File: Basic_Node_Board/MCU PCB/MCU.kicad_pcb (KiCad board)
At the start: 4 copper layers, 100 x 100 mm, 31 parts, among them J1 Conn_01x02, J2 Conn_01x06_Socket, J4 Conn_01x02_Pin, J5 Conn_01x03_Socket, U2 ESP32-DEVKIT-C, U3 TPS54560BQDDARQ1, U6 TJA1050T/CM,118

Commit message: fixed the buck converter
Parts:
- added REF**: MountingHole_3.2mm_M3_DIN965_Pad_TopBottom, MountingHole:MountingHole_3.2mm_M3_DIN965_Pad_TopBottom, F.Cu at (39.8, 120.8)
- added REF**: MountingHole_3.2mm_M3_DIN965_Pad_TopBottom, MountingHole:MountingHole_3.2mm_M3_DIN965_Pad_TopBottom, F.Cu at (131.8, 28.5)
- added REF**: MountingHole_3.2mm_M3_DIN965_Pad_TopBottom, MountingHole:MountingHole_3.2mm_M3_DIN965_Pad_TopBottom, F.Cu at (131.0, 120.2)
- moved L1 13.8 mm to (76.0, 41.8)
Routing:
- net Net-(U3-FB): track 34.2 -> 52.6 mm, vias 2 -> 3
- net Net-(U3-SW): track 17.8 -> 24.6 mm, vias 0 -> 2
- net 5.3V OUT: track 264.1 -> 270.0 mm, vias 4 -> 6
- net Net-(J3-Pin_12): track 120.4 -> 116.8 mm

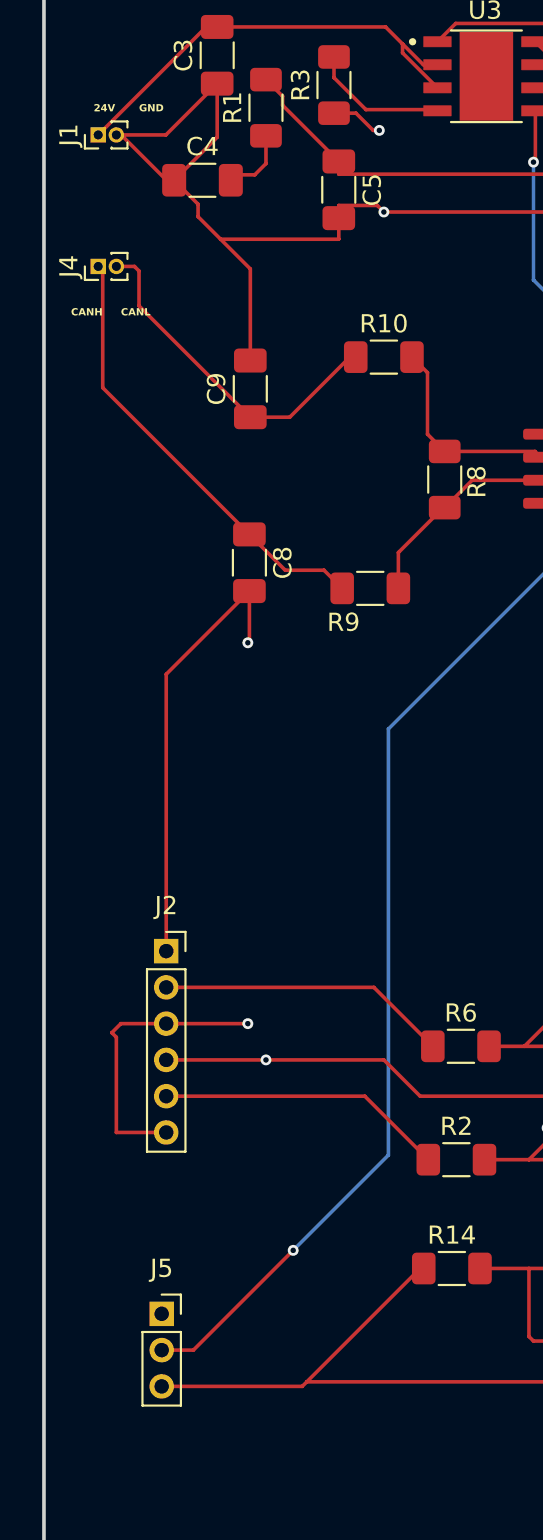
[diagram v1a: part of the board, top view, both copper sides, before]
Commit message: fixed the pin and connectors for the mcu board
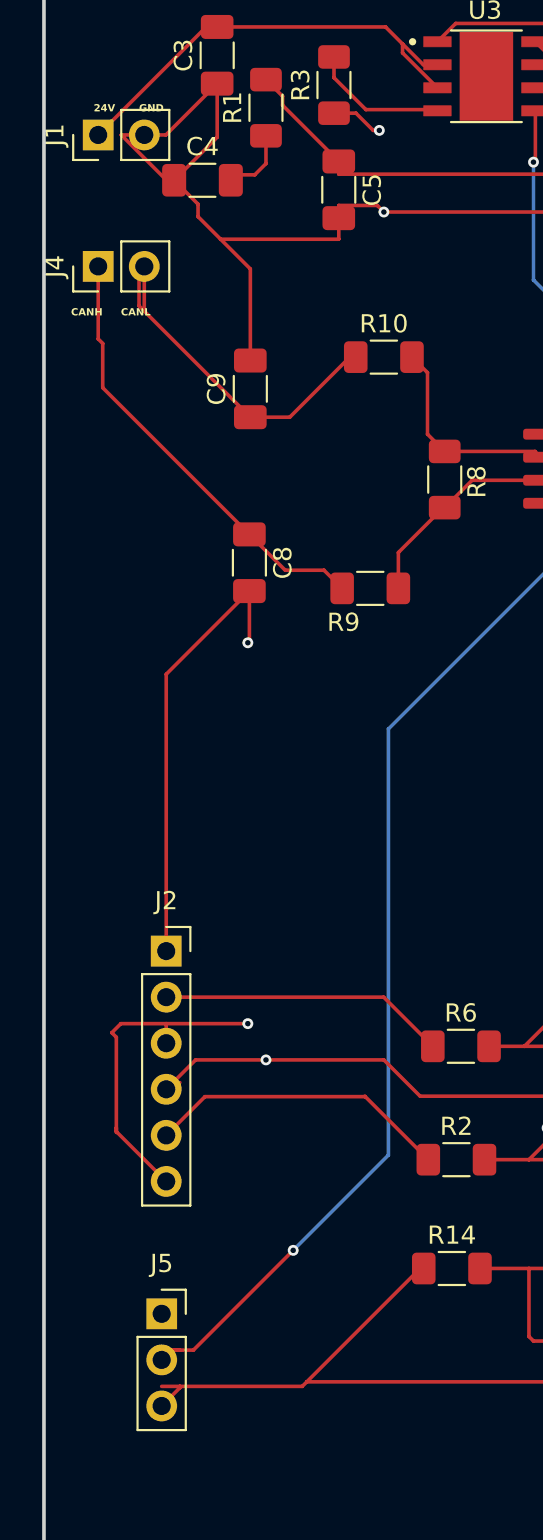
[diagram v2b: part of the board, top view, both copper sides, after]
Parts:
- J1, J4: footprint Connector_PinHeader_1.00mm:PinHeader_1x02_P1.00mm_Vertical -> Connector_PinHeader_2.54mm:PinHeader_1x02_P2.54mm_Vertical
- J2: footprint Connector_PinSocket_2.00mm:PinSocket_1x06_P2.00mm_Vertical -> Connector_PinSocket_2.54mm:PinSocket_1x06_P2.54mm_Vertical
- J5: footprint Connector_PinSocket_2.00mm:PinSocket_1x03_P2.00mm_Vertical -> Connector_PinSocket_2.54mm:PinSocket_1x03_P2.54mm_Vertical
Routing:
- net 5.3V OUT: track 270.0 -> 273.9 mm
- net /CANL: track 19.1 -> 20.6 mm
- net Net-(J5-Pin_2): track 95.0 -> 96.2 mm
- net Net-(J2-Pin_5): track 15.9 -> 16.8 mm
- net GND: track 323.9 -> 324.7 mm
- net Net-(J2-Pin_2): track 16.0 -> 16.6 mm
